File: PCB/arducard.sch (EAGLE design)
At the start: 92 parts, among them J1 USB MICRO, Q1 BC817-16LT1SMD, Q2 DMG2301U-7, Q3 2N7002, Q4 BSS84, Q5 2N7002, Q6 2N7002, Q7 2N7002, Q8 BSS84, Q9 DMG2301U-7, U1 microSD, U2 ATMEGA32U4-XUAU, U4 DS3234, Y1 8MHz KX-7

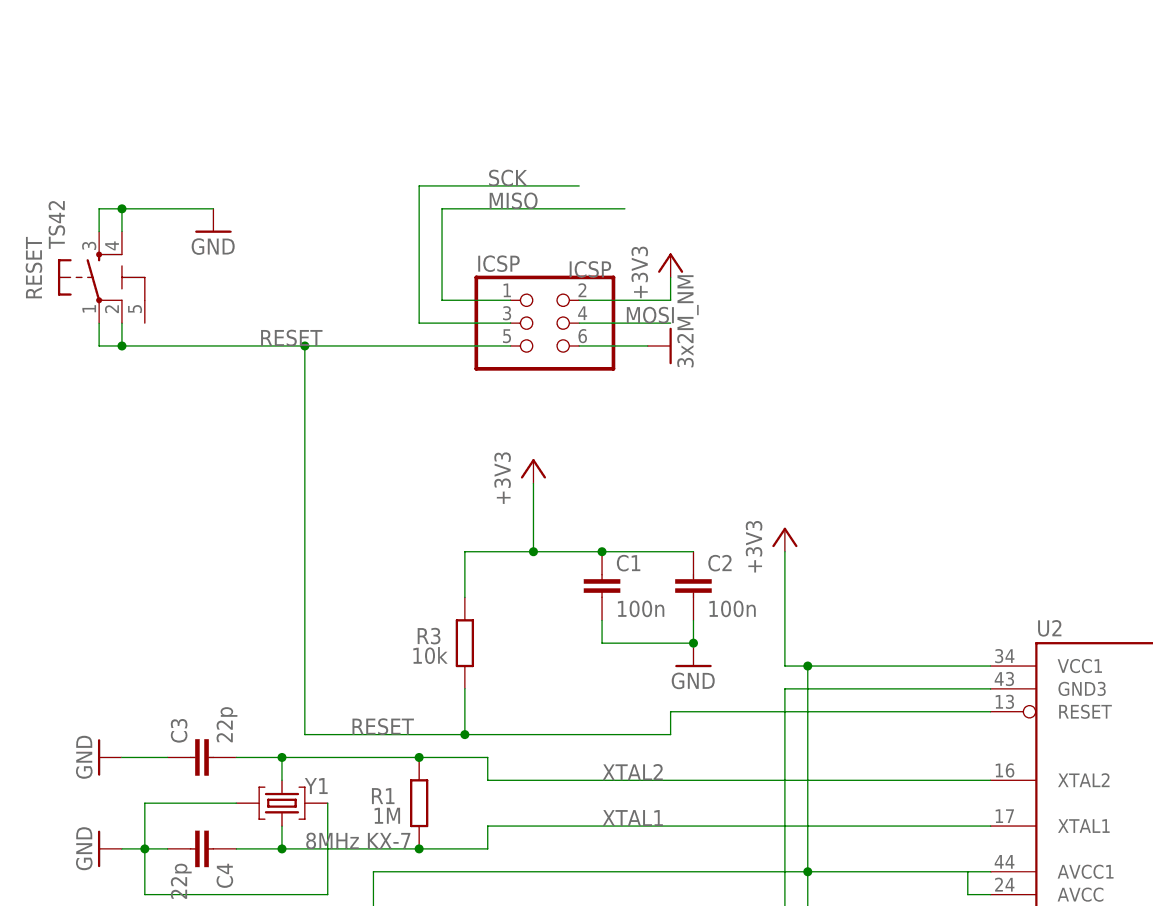
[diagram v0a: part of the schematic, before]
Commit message: removed reset switch
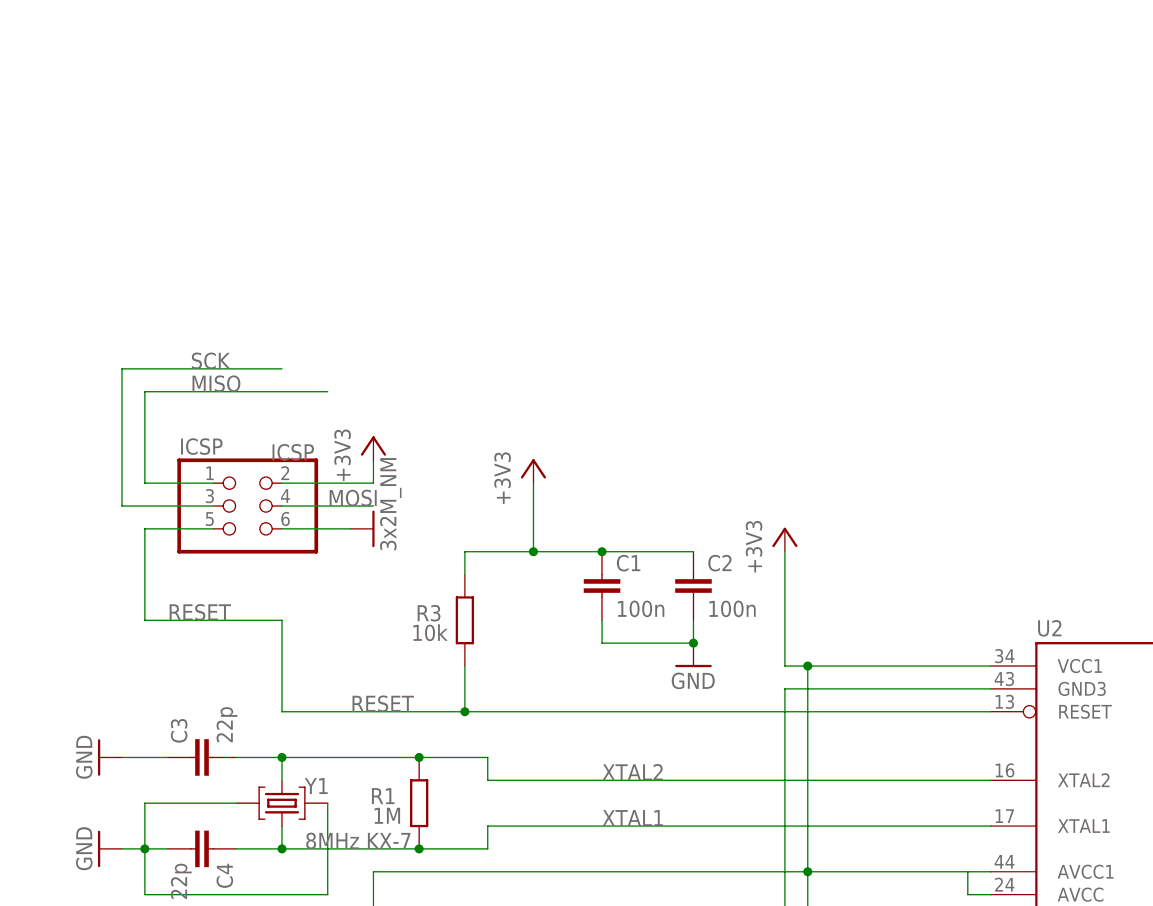
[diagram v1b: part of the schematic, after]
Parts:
- removed RESET: TS42, SmartPrj:TS42
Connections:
- net GND: no longer RESET.3, RESET.4
- net RESET: no longer RESET.1, RESET.2
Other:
- moved on the sheet: ICSP, R3
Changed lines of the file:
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@@
 <part name="ICSP" library="SmartPrj" deviceset="PINHD-2X3" device="" value="ICSP"/>
 <part name="GND1" library="supply1" deviceset="GND" device="" value="3x2M_NM"/>
-<part name="GND12" library="supply1" deviceset="GND" device=""/>
 <part name="R1" library="SmartPrj" deviceset="R-EU_" device="R0603" value="1M"/>
 <part name="U$25" library="MyPOW" deviceset="VUSB" device=""/>
@@
 <part name="C2" library="SmartPrj" deviceset="C-EU" device="C0603" value="100n"/>
 <part name="C1" library="SmartPrj" deviceset="C-EU" device="C0603" value="100n"/>
-<part name="RESET" library="SmartPrj" deviceset="TS42" device=""/>
 <part name="C3" library="SmartPrj" deviceset="C-EU" device="C0603" value="22p"/>
 <part name="C4" library="SmartPrj" deviceset="C-EU" device="C0603" value="22p"/>
@@
 </plain>
 <instances>
-<instance part="ICSP" gate="A" x="60.96" y="162.56" smashed="yes">
-<attribute name="NAME" x="54.61" y="168.275" size="1.778" layer="95"/>
-<attribute name="VALUE" x="64.77" y="167.64" size="1.778" layer="96"/>
-</instance>
-<instance part="GND1" gate="1" x="76.2" y="160.02" rot="R90"/>
-<instance part="GND12" gate="1" x="25.4" y="172.72"/>
+<instance part="ICSP" gate="A" x="27.94" y="142.24" smashed="yes">
+<attribute name="NAME" x="21.59" y="147.955" size="1.778" layer="95"/>
+<attribute name="VALUE" x="31.75" y="147.32" size="1.778" layer="96"/>
+</instance>
+<instance part="GND1" gate="1" x="43.18" y="139.7" rot="R90"/>
 <instance part="R1" gate="G$1" x="48.26" y="109.22" smashed="yes" rot="R90">
 <attribute name="NAME" x="45.72" y="110.8964" size="1.778" layer="95" rot="R180"/>
@@
 <instance part="C2" gate="G$1" x="78.74" y="134.62"/>
 <instance part="C1" gate="G$1" x="68.58" y="134.62"/>
-<instance part="RESET" gate="G$1" x="12.7" y="167.64"/>
 <instance part="C3" gate="G$1" x="22.86" y="114.3" rot="R90"/>
 <instance part="C4" gate="G$1" x="25.4" y="104.14" rot="R270"/>
@@
 </instance>
 <instance part="C5" gate="G$1" x="396.24" y="35.56"/>
-<instance part="+3V4" gate="G$1" x="76.2" y="170.18"/>
+<instance part="+3V4" gate="G$1" x="43.18" y="149.86"/>
 <instance part="IC1" gate="G1" x="541.02" y="119.38"/>
 <instance part="L1" gate="G$1" x="561.34" y="124.46" rot="R90"/>
@@
 <instance part="U$5" gate="G$1" x="289.56" y="162.56"/>
 <instance part="C8" gate="G$1" x="347.98" y="60.96" rot="MR180"/>
-<instance part="R3" gate="G$1" x="53.34" y="127" smashed="yes" rot="R90">
-<attribute name="NAME" x="50.8" y="128.6764" size="1.778" layer="95" rot="R180"/>
-<attribute name="VALUE" x="51.435" y="126.492" size="1.778" layer="96" rot="R180"/>
+<instance part="R3" gate="G$1" x="53.34" y="129.54" smashed="yes" rot="R90">
+<attribute name="NAME" x="50.8" y="131.2164" size="1.778" layer="95" rot="R180"/>
+<attribute name="VALUE" x="51.435" y="129.032" size="1.778" layer="96" rot="R180"/>
 </instance>
 <instance part="R4" gate="G$1" x="335.28" y="83.82" smashed="yes">
@@
 <net name="GND" class="2">
 <segment>
-<wire x1="73.66" y1="160.02" x2="66.04" y2="160.02" width="0.1524" layer="91"/>
+<wire x1="40.64" y1="139.7" x2="33.02" y2="139.7" width="0.1524" layer="91"/>
 <pinref part="GND1" gate="1" pin="GND"/>
 <pinref part="ICSP" gate="A" pin="6"/>
-</segment>
-<segment>
-<wire x1="12.7" y1="172.72" x2="12.7" y2="175.26" width="0.1524" layer="91"/>
-<wire x1="12.7" y1="175.26" x2="15.24" y2="175.26" width="0.1524" layer="91"/>
-<wire x1="15.24" y1="175.26" x2="25.4" y2="175.26" width="0.1524" layer="91"/>
-<wire x1="15.24" y1="172.72" x2="15.24" y2="175.26" width="0.1524" layer="91"/>
-<junction x="15.24" y="175.26"/>
-<pinref part="GND12" gate="1" pin="GND"/>
-<pinref part="RESET" gate="G$1" pin="3"/>
-<pinref part="RESET" gate="G$1" pin="4"/>
 </segment>
 <segment>
@@
 <net name="RESET" class="0">
 <segment>
-<wire x1="58.42" y1="160.02" x2="35.56" y2="160.02" width="0.1524" layer="91"/>
-<wire x1="35.56" y1="160.02" x2="35.56" y2="116.84" width="0.1524" layer="91"/>
-<wire x1="111.76" y1="119.38" x2="76.2" y2="119.38" width="0.1524" layer="91"/>
-<wire x1="76.2" y1="119.38" x2="76.2" y2="116.84" width="0.1524" layer="91"/>
-<wire x1="53.34" y1="116.84" x2="76.2" y2="116.84" width="0.1524" layer="91"/>
-<wire x1="53.34" y1="121.92" x2="53.34" y2="116.84" width="0.1524" layer="91"/>
-<wire x1="35.56" y1="116.84" x2="53.34" y2="116.84" width="0.1524" layer="91"/>
-<wire x1="12.7" y1="162.56" x2="12.7" y2="160.02" width="0.1524" layer="91"/>
-<wire x1="12.7" y1="160.02" x2="15.24" y2="160.02" width="0.1524" layer="91"/>
-<wire x1="15.24" y1="160.02" x2="35.56" y2="160.02" width="0.1524" layer="91"/>
-<wire x1="15.24" y1="162.56" x2="15.24" y2="160.02" width="0.1524" layer="91"/>
-<junction x="35.56" y="160.02"/>
-<junction x="53.34" y="116.84"/>
-<junction x="15.24" y="160.02"/>
-<label x="30.48" y="160.02" size="1.778" layer="95"/>
-<label x="40.64" y="116.84" size="1.778" layer="95"/>
+<wire x1="25.4" y1="139.7" x2="17.78" y2="139.7" width="0.1524" layer="91"/>
+<wire x1="17.78" y1="139.7" x2="17.78" y2="129.54" width="0.1524" layer="91"/>
+<wire x1="17.78" y1="129.54" x2="33.02" y2="129.54" width="0.1524" layer="91"/>
+<wire x1="33.02" y1="129.54" x2="33.02" y2="119.38" width="0.1524" layer="91"/>
+<wire x1="111.76" y1="119.38" x2="53.34" y2="119.38" width="0.1524" layer="91"/>
+<wire x1="53.34" y1="124.46" x2="53.34" y2="119.38" width="0.1524" layer="91"/>
+<wire x1="33.02" y1="119.38" x2="53.34" y2="119.38" width="0.1524" layer="91"/>
+<junction x="53.34" y="119.38"/>
+<label x="20.32" y="129.54" size="1.778" layer="95"/>
+<label x="40.64" y="119.38" size="1.778" layer="95"/>
 <pinref part="ICSP" gate="A" pin="5"/>
-<pinref part="RESET" gate="G$1" pin="1"/>
-<pinref part="RESET" gate="G$1" pin="2"/>
 <pinref part="U2" gate="G$1" pin="RESET"/>
 <pinref part="R3" gate="G$1" pin="1"/>
@@
 <net name="SCK" class="0">
 <segment>
-<wire x1="58.42" y1="162.56" x2="48.26" y2="162.56" width="0.1524" layer="91"/>
-<wire x1="48.26" y1="162.56" x2="48.26" y2="177.8" width="0.1524" layer="91"/>
-<wire x1="48.26" y1="177.8" x2="66.04" y2="177.8" width="0.1524" layer="91"/>
-<label x="55.88" y="177.8" size="1.778" layer="95"/>
+<wire x1="25.4" y1="142.24" x2="15.24" y2="142.24" width="0.1524" layer="91"/>
+<wire x1="15.24" y1="142.24" x2="15.24" y2="157.48" width="0.1524" layer="91"/>
+<wire x1="15.24" y1="157.48" x2="33.02" y2="157.48" width="0.1524" layer="91"/>
+<label x="22.86" y="157.48" size="1.778" layer="95"/>
 <pinref part="ICSP" gate="A" pin="3"/>
 </segment>
@@
 <net name="MISO" class="0">
 <segment>
-<wire x1="58.42" y1="165.1" x2="50.8" y2="165.1" width="0.1524" layer="91"/>
-<wire x1="50.8" y1="165.1" x2="50.8" y2="175.26" width="0.1524" layer="91"/>
-<wire x1="50.8" y1="175.26" x2="71.12" y2="175.26" width="0.1524" layer="91"/>
-<label x="55.88" y="175.26" size="1.778" layer="95"/>
+<wire x1="25.4" y1="144.78" x2="17.78" y2="144.78" width="0.1524" layer="91"/>
+<wire x1="17.78" y1="144.78" x2="17.78" y2="154.94" width="0.1524" layer="91"/>
+<wire x1="17.78" y1="154.94" x2="38.1" y2="154.94" width="0.1524" layer="91"/>
+<label x="22.86" y="154.94" size="1.778" layer="95"/>
 <pinref part="ICSP" gate="A" pin="1"/>
 </segment>
@@
 <net name="MOSI" class="0">
 <segment>
-<wire x1="66.04" y1="162.56" x2="76.2" y2="162.56" width="0.1524" layer="91"/>
-<label x="71.12" y="162.56" size="1.778" layer="95"/>
+<wire x1="33.02" y1="142.24" x2="43.18" y2="142.24" width="0.1524" layer="91"/>
+<label x="38.1" y="142.24" size="1.778" layer="95"/>
 <pinref part="ICSP" gate="A" pin="4"/>
 </segment>
@@
 <wire x1="53.34" y1="137.16" x2="60.96" y2="137.16" width="0.1524" layer="91"/>
 <wire x1="60.96" y1="137.16" x2="68.58" y2="137.16" width="0.1524" layer="91"/>
-<wire x1="53.34" y1="132.08" x2="53.34" y2="137.16" width="0.1524" layer="91"/>
+<wire x1="53.34" y1="134.62" x2="53.34" y2="137.16" width="0.1524" layer="91"/>
 <junction x="68.58" y="137.16"/>
 <pinref part="C2" gate="G$1" pin="1"/>
@@
 </segment>
 <segment>
-<wire x1="76.2" y1="167.64" x2="76.2" y2="165.1" width="0.1524" layer="91"/>
-<wire x1="76.2" y1="165.1" x2="66.04" y2="165.1" width="0.1524" layer="91"/>
+<wire x1="43.18" y1="147.32" x2="43.18" y2="144.78" width="0.1524" layer="91"/>
+<wire x1="43.18" y1="144.78" x2="33.02" y2="144.78" width="0.1524" layer="91"/>
 <pinref part="ICSP" gate="A" pin="2"/>
 <pinref part="+3V4" gate="G$1" pin="+3V3"/>

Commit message: added coin cell battery
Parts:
- added U$7: LIR2016, arducard-coincell:LIR2016
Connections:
- net BATT_RAW: now also U$7.+
- net GND: now also U$7.–
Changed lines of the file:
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@@
 <part name="U$1" library="arducard-switch" deviceset="EVQ-PUA" device=""/>
 <part name="R27" library="SmartPrj" deviceset="R-EU_" device="R0603" value="10k"/>
+<part name="U$7" library="arducard-coincell" deviceset="LIR2016" device=""/>
+<part name="GND6" library="supply1" deviceset="GND" device=""/>
 </parts>
 <sheets>
@@
 <attribute name="VALUE" x="225.552" y="159.385" size="1.778" layer="96" rot="R90"/>
 </instance>
+<instance part="U$7" gate="G$1" x="482.6" y="55.88"/>
+<instance part="GND6" gate="1" x="454.66" y="58.42" rot="R270"/>
 </instances>
 <busses>
@@
 <junction x="236.22" y="157.48"/>
 </segment>
+<segment>
+<pinref part="U$7" gate="G$1" pin="–"/>
+<pinref part="GND6" gate="1" pin="GND"/>
+<wire x1="472.44" y1="58.42" x2="457.2" y2="58.42" width="0.1524" layer="91"/>
+</segment>
 </net>
 <net name="RESET" class="0">
 <segment>
 <wire x1="25.4" y1="139.7" x2="17.78" y2="139.7" width="0.1524" layer="91"/>
-<wire x1="17.78" y1="139.7" x2="17.78" y2="129.54" width="0.1524" layer="91"/>
-<wire x1="17.78" y1="129.54" x2="33.02" y2="129.54" width="0.1524" layer="91"/>
-<wire x1="33.02" y1="129.54" x2="33.02" y2="119.38" width="0.1524" layer="91"/>
+<wire x1="17.78" y1="139.7" x2="17.78" y2="121.92" width="0.1524" layer="91"/>
+<wire x1="17.78" y1="121.92" x2="33.02" y2="121.92" width="0.1524" layer="91"/>
+<wire x1="33.02" y1="121.92" x2="33.02" y2="119.38" width="0.1524" layer="91"/>
 <wire x1="111.76" y1="119.38" x2="53.34" y2="119.38" width="0.1524" layer="91"/>
 <wire x1="53.34" y1="124.46" x2="53.34" y2="119.38" width="0.1524" layer="91"/>
 <wire x1="33.02" y1="119.38" x2="53.34" y2="119.38" width="0.1524" layer="91"/>
 <junction x="53.34" y="119.38"/>
-<label x="20.32" y="129.54" size="1.778" layer="95"/>
 <label x="40.64" y="119.38" size="1.778" layer="95"/>
 <pinref part="ICSP" gate="A" pin="5"/>
@@
 <label x="457.2" y="88.9" size="1.778" layer="95"/>
 </segment>
-</net>
+<segment>
+<pinref part="U$7" gate="G$1" pin="+"/>
+<wire x1="472.44" y1="53.34" x2="457.2" y2="53.34" width="0.1524" layer="91"/>
+<label x="457.2" y="53.34" size="1.778" layer="95"/>
+</segment>
+</net>

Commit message: changed RTC to DS1343
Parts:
- removed U4: DS3234, SparkFun:DS3234
- added U$10: DS1343, arducard-rtc:DS1343
- added U$6: LIR2016, arducard-coincell:LIR2016
- U$7: value LIR2016 -> SSP-T7-F; device arducard-coincell:LIR2016 -> arducard-rtc:SSP-T7-F
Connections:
- new net N$17: U$10.X2, U$7.P$1
- new net N$4: U$10.X1, U$7.P$2
- new net SCLK: U$10.SCLK
- net +3V3: now also U$10.SERMODE, U$10.VCC; no longer U4.VCC
- net B4: now also U2.(ADC11/PCINT4)PB4; no longer U2.(PCINT7/OC0A/OC1C/#RTS)PB7
- net BATTSENS: now also U2.(ADC1)PF1; no longer U2.(ADC5/TMS)PF5
- net BATTSENS_EN: now also U2.(ADC0)PF0; no longer U2.(ADC4/TCK)PF4
- net BATT_RAW: now also U$6.+; no longer U$7.+
- net BORDER_CONTROL: now also U2.(ADC7/TDI)PF7
- net CHGSTAT: now also U2.(SS/PCINT0)PB0; no longer U2.(ADC6/TDO)PF6
- net DISCHARGE: now also U2.(ADC5/TMS)PF5
- net GND: now also U$10.GND, U$6.–; no longer U$7.–, U4.GND, U4.GND@10, U4.GND@11, U4.GND@12, U4.GND@13, U4.GND@14, U4.GND@2, U4.GND@7, U4.GND@8, U4.GND@9
- net MISO: now also U$10.SDO; no longer U4.DOUT
- net MOSI: now also U$10.SDI; no longer U4.DIN
- net PANEL_ON: now also U2.(ADC6/TDO)PF6
- net PWM: now also U2.(PCINT7/OC0A/OC1C/#RTS)PB7
- net RTC_CS: now also U$10.CE; no longer U4.CS
- net RTC_INT: now also U$10./INT0; no longer U4.INT/SQW
- net SCK: no longer U4.SCLK@18, U4.SCLK@20
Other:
- moved on the sheet: C14, R19

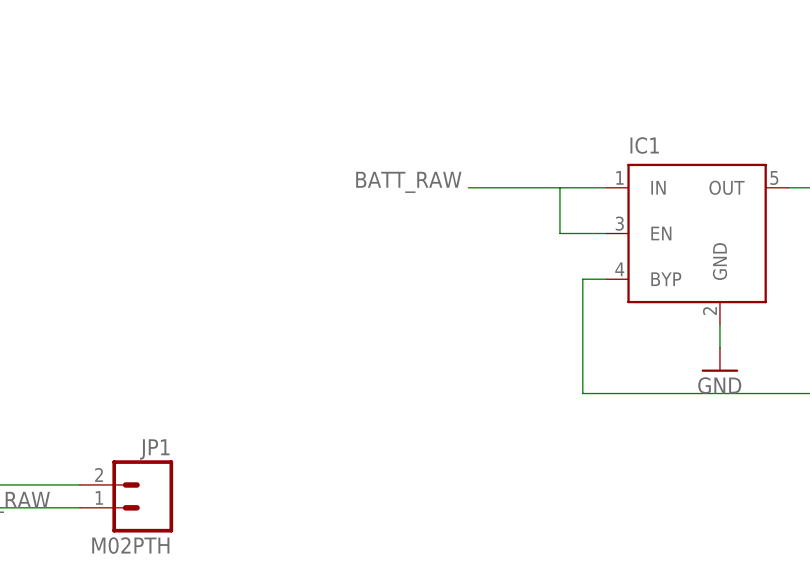
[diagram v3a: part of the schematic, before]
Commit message: added bypass cap to vreg input
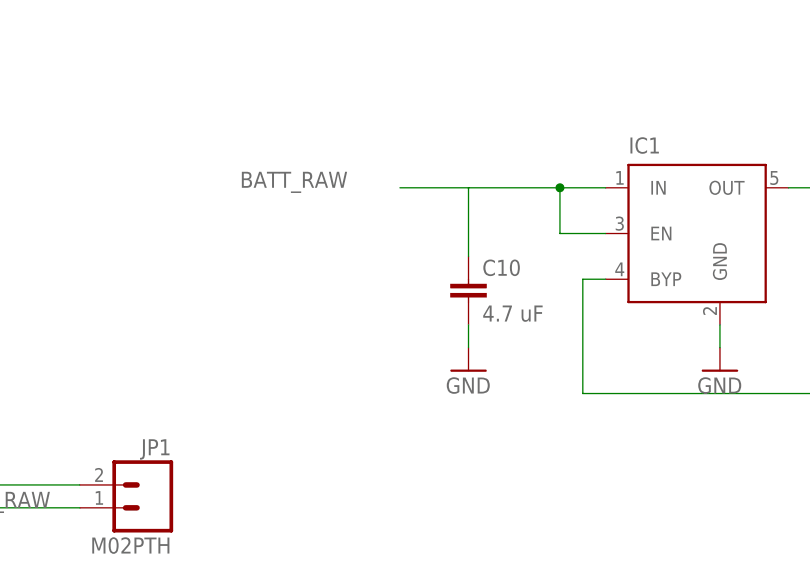
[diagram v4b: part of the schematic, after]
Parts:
- added C10: 4.7 uF, SmartPrj:C-EUC0603
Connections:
- net BATT_RAW: now also C10.1
- net GND: now also C10.2
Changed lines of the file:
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@@
 <part name="+3V7" library="supply1" deviceset="+3V3" device=""/>
 <part name="GND12" library="supply1" deviceset="GND" device=""/>
+<part name="C10" library="SmartPrj" deviceset="C-EU" device="C0603" value="4.7 uF"/>
+<part name="GND17" library="supply1" deviceset="GND" device=""/>
 </parts>
 <sheets>
@@
 <instance part="+3V7" gate="G$1" x="657.86" y="68.58" rot="R270"/>
 <instance part="GND12" gate="1" x="596.9" y="38.1"/>
+<instance part="C10" gate="G$1" x="515.62" y="114.3"/>
+<instance part="GND17" gate="1" x="515.62" y="104.14"/>
 </instances>
 <busses>
@@
 <junction x="596.9" y="43.18"/>
 </segment>
+<segment>
+<pinref part="GND17" gate="1" pin="GND"/>
+<pinref part="C10" gate="G$1" pin="2"/>
+<wire x1="515.62" y1="106.68" x2="515.62" y2="109.22" width="0.1524" layer="91"/>
+</segment>
 </net>
 <net name="RESET" class="0">
@@
 <wire x1="525.78" y1="119.38" x2="525.78" y2="124.46" width="0.1524" layer="91"/>
 <wire x1="525.78" y1="124.46" x2="515.62" y2="124.46" width="0.1524" layer="91"/>
-<label x="502.92" y="124.46" size="1.778" layer="95"/>
-</segment>
-<segment>
+<label x="490.22" y="124.46" size="1.778" layer="95"/>
+<junction x="525.78" y="124.46"/>
+<pinref part="C10" gate="G$1" pin="1"/>
+<wire x1="515.62" y1="124.46" x2="508" y2="124.46" width="0.1524" layer="91"/>
+<wire x1="515.62" y1="116.84" x2="515.62" y2="124.46" width="0.1524" layer="91"/>
+</segment>
+<segment>

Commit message: organized schematic layout
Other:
- note added: "Arducard"
- note added: "Battery Charger"
- note added: "Battery Connector"
- note added: "Battery Level Sensing"
- note added: "FRAM"
- note added: "MicroSD Connector"
- note added: "Microcontroller"
- note added: "Real-Time Clock"
- note added: "Tactile Buttons"
- note added: "USB Micro Connector"
- note added: "Voltage Regulator"
- note added: "ePaper Display"
- note removed: "USB"
- moved on the sheet: C1, C10, C11, C12, C13, C14, C15, C16, C17, C18, C19, C2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
